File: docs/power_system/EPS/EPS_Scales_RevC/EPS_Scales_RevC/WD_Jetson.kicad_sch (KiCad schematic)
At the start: 40 parts, among them J6 Breakout, J7 Breakout, U3 TLV1704

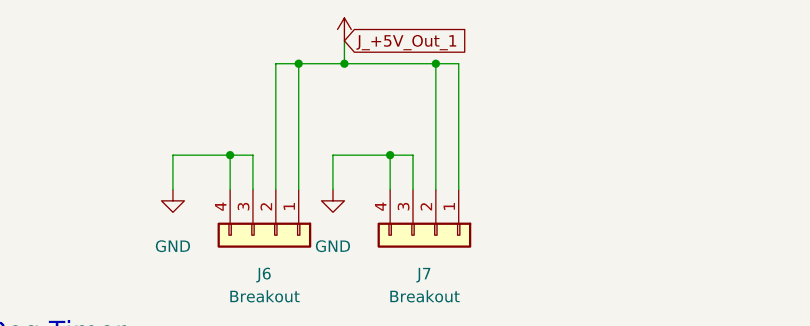
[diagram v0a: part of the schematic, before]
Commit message: Calculations
Lots of behind the scenes stuff going on. Ran through calculations for the Load Switch, Switching Regulator and clock for the jetson using the information from each datasheet. Having to modify these parameters for each subsystem is time consuming as each one requires new calculations. Once this bit is done the schematic will be done, leading to layout. Aiming for thursday Layout.
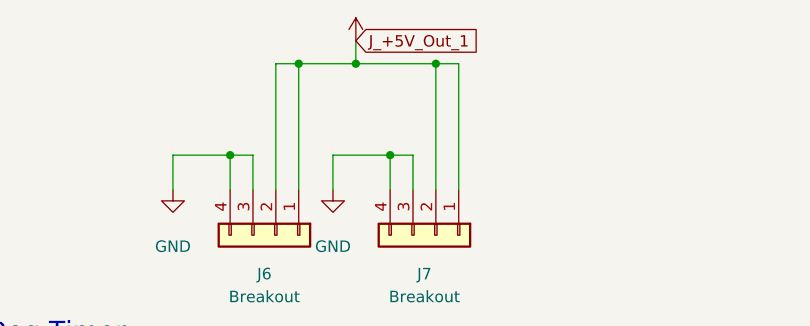
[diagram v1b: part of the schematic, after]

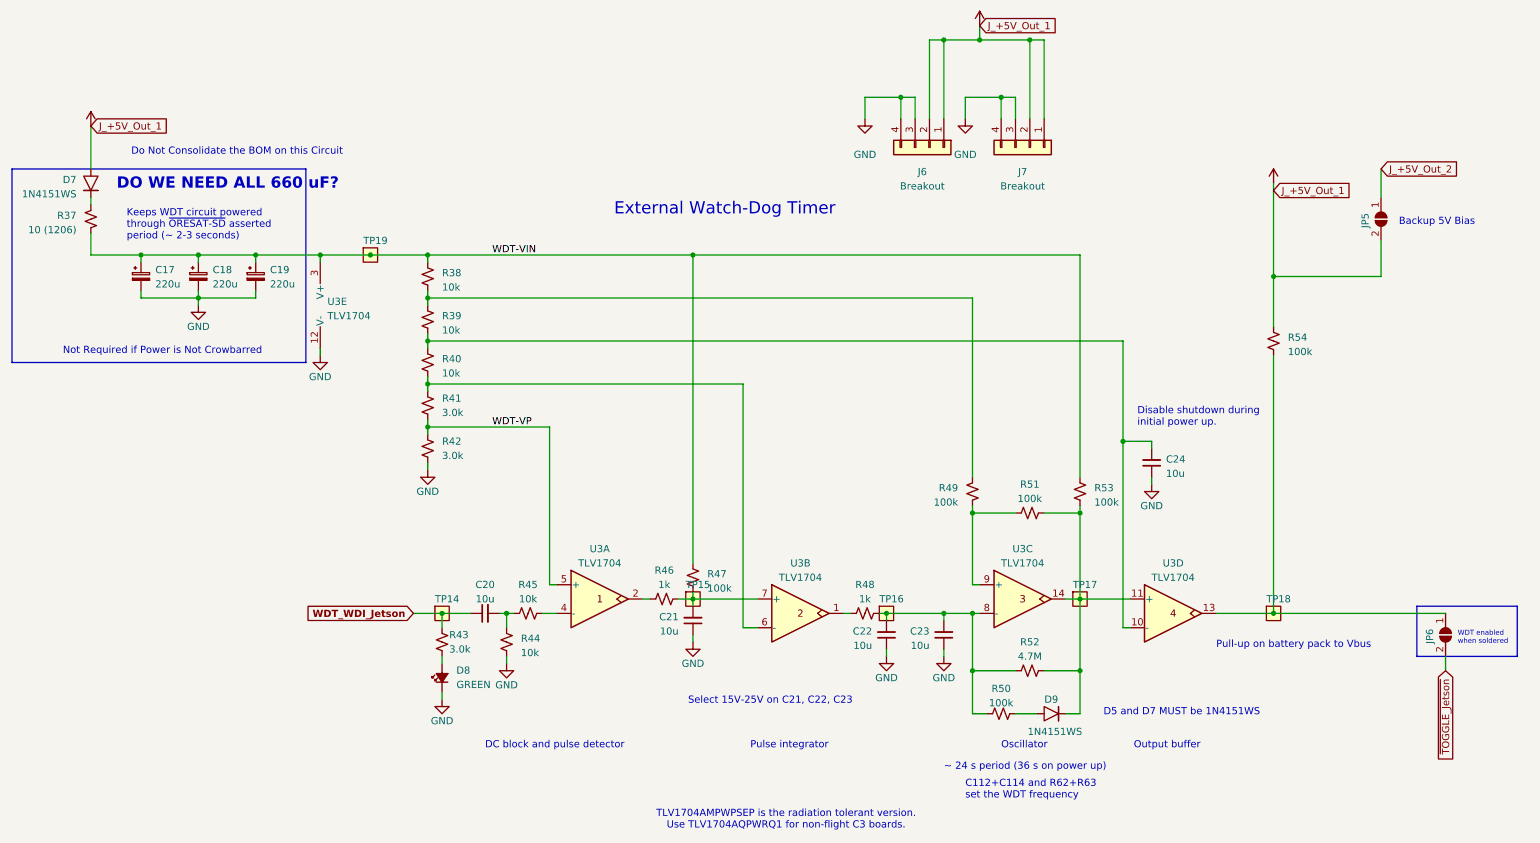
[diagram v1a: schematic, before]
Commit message: Rev C. Schematic 90 % Complete
All EPS components for each subsystem implemented. Only errors and warning are relating to missing peripheral connections and connectors which will be discussed tomorrow when I go to the lab.
Calculations are done as well.
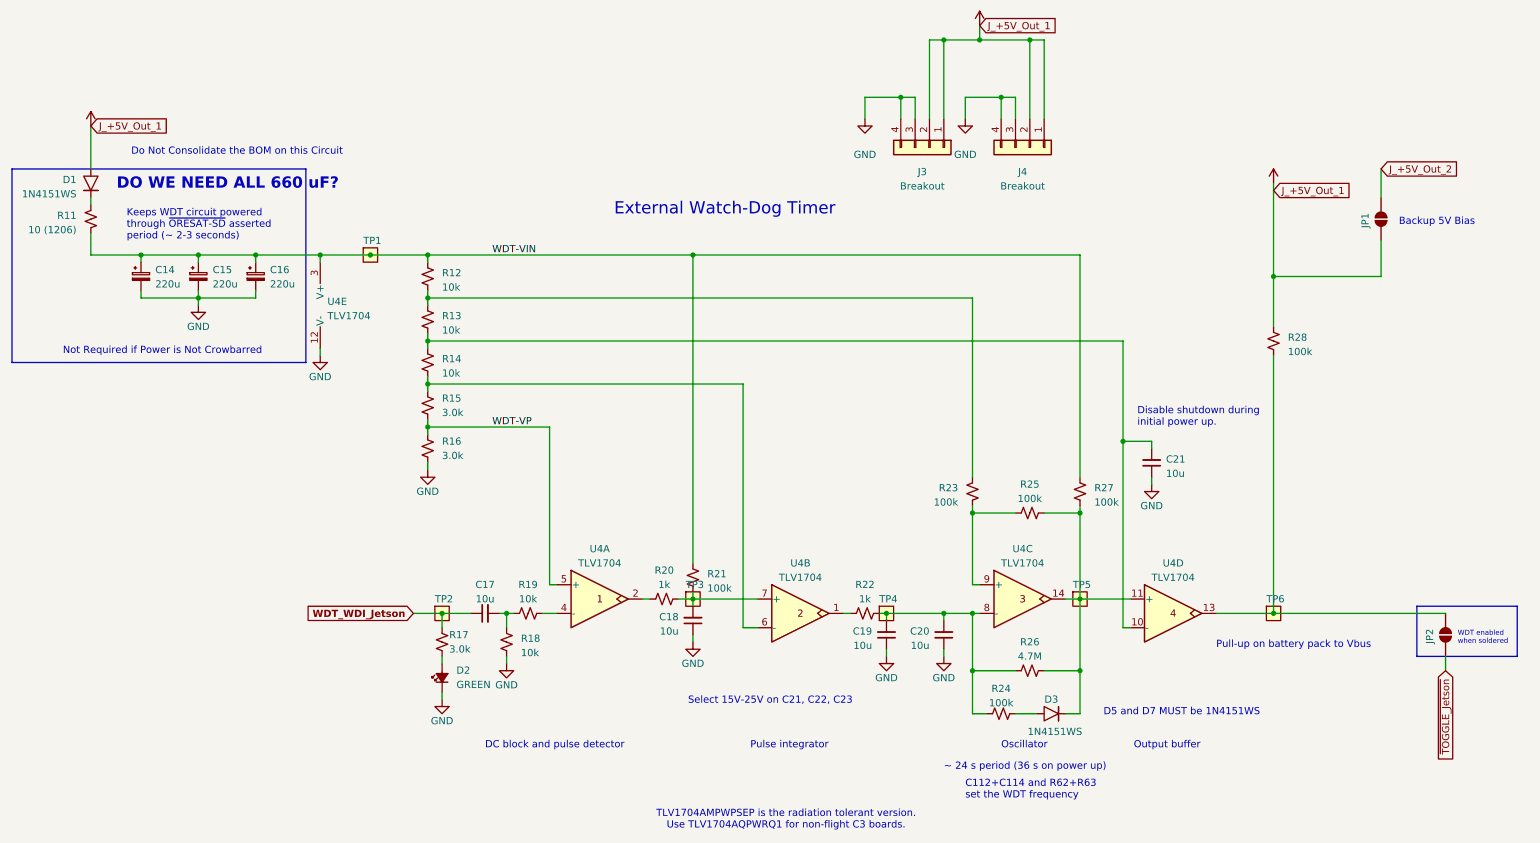
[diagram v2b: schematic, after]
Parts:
- renumbered C17 to C14, C18 to C15, C19 to C16, C20 to C17, C21 to C18, C22 to C19, C23 to C20, C24 to C21, D7 to D1, D8 to D2, D9 to D3, J6 to J3, J7 to J4, JP5 to JP1, JP6 to JP2, R37 to R11, R38 to R12, R39 to R13, R40 to R14, R41 to R15, R42 to R16, R43 to R17, R44 to R18, R45 to R19, R46 to R20, R47 to R21, R48 to R22, R49 to R23, R50 to R24, R51 to R25, R52 to R26, R53 to R27, R54 to R28, TP19 to TP1, TP14 to TP2, TP15 to TP3, TP16 to TP4, TP17 to TP5, TP18 to TP6, U3 to U4

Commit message: Added Dummy Boards & XNOR functionality
Almost done with Dummy boards, just need to link some gecko footprints to the schematic symbol pins and layout can begin
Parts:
- D1, D3: symbol oresat-diodes:1N4151WS-HE3 -> Device:D
- J4: footprint FC_DEV_BOARD:JST_BM04B-SRSS-TB(LF)(SN) -> Connector_PinHeader_2.54mm:PinHeader_1x04_P2.54mm_Vertical
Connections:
- net J_+5V_Out_2 is gone; now on net +5V_ROUT3: JP1.1 (A)
- net ~{TOGGLE_Jetson} renamed ~{WD_TOGGLE_Jetson}
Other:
- note added: "D1 and D7 MUST be 1N4151WS"
- note removed: "D5 and D7 MUST be 1N4151WS"
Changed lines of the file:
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@@
 		)
 	)
-	(text "D5 and D7 MUST be 1N4151WS"
+	(text "D1 and D7 MUST be 1N4151WS"
 		(exclude_from_sim no)
 		(at 222.504 140.716 0)
@@
 	(wire
 		(pts
-			(xy 201.93 140.97) (xy 204.47 140.97)
-		)
-		(stroke
-			(width 0)
-			(type default)
-		)
-	)
-	(wire
-		(pts
 			(xy 88.9 90.17) (xy 88.9 91.44)
 		)
@@
 	(wire
 		(pts
-			(xy 38.1 59.69) (xy 48.26 59.69)
+			(xy 193.04 140.97) (xy 194.31 140.97)
 		)
 		(stroke
@@
 	(wire
 		(pts
-			(xy 177.8 35.56) (xy 177.8 21.59)
+			(xy 38.1 59.69) (xy 48.26 59.69)
 		)
 		(stroke
@@
 	(wire
 		(pts
-			(xy 29.21 36.83) (xy 29.21 44.45)
+			(xy 177.8 35.56) (xy 177.8 21.59)
 		)
 		(stroke
@@
 	(wire
 		(pts
-			(xy 238.76 46.99) (xy 238.76 63.5)
+			(xy 238.76 43.18) (xy 238.76 63.5)
 		)
 		(stroke
@@
 	(wire
 		(pts
+			(xy 201.93 140.97) (xy 204.47 140.97)
+		)
+		(stroke
+			(width 0)
+			(type default)
+		)
+	)
+	(wire
+		(pts
 			(xy 185.42 99.06) (xy 185.42 67.31)
 		)
@@
 	(wire
 		(pts
-			(xy 29.21 49.53) (xy 29.21 50.8)
+			(xy 58.42 60.96) (xy 58.42 59.69)
 		)
 		(stroke
@@
 	(wire
 		(pts
-			(xy 58.42 60.96) (xy 58.42 59.69)
+			(xy 193.04 133.35) (xy 185.42 133.35)
 		)
 		(stroke
@@
 	(wire
 		(pts
-			(xy 193.04 133.35) (xy 185.42 133.35)
+			(xy 69.85 59.69) (xy 78.74 59.69)
 		)
 		(stroke
@@
 	(wire
 		(pts
-			(xy 69.85 59.69) (xy 78.74 59.69)
+			(xy 29.21 36.83) (xy 29.21 41.91)
 		)
 		(stroke
@@
 	(wire
 		(pts
+			(xy 29.21 49.53) (xy 29.21 50.8)
+		)
+		(stroke
+			(width 0)
+			(type default)
+		)
+	)
+	(wire
+		(pts
 			(xy 212.09 74.93) (xy 212.09 92.71)
 		)
@@
 		)
 	)
-	(wire
-		(pts
-			(xy 193.04 140.97) (xy 196.85 140.97)
-		)
-		(stroke
-			(width 0)
-			(type default)
-		)
-	)
 	(polyline
 		(pts
@@
 		)
 	)
-	(global_label "J_+5V_Out_2"
+	(global_label "~{WD_TOGGLE_Jetson}"
 		(shape input)
-		(at 257.81 44.45 0)
+		(at 269.24 133.35 270)
 		(fields_autoplaced yes)
 		(effects
@@
 				(size 1.27 1.27)
 			)
-			(justify left)
+			(justify right)
 		)
 		(property "Intersheetrefs" "${INTERSHEET_REFS}"
-			(at 272.9508 44.45 0)
+			(at 269.24 154.115 90)
 			(effects
 				(font
 					(size 1.27 1.27)
 				)
-				(justify left)
+				(justify right)
 				(hide yes)
 			)
 		)
 	)
-	(global_label "~{TOGGLE_Jetson}"
+	(global_label "J_+5V_Out_1"
 		(shape input)
-		(at 269.24 133.35 270)
+		(at 186.69 19.05 0)
 		(fields_autoplaced yes)
 		(effects
@@
 				(size 1.27 1.27)
 			)
-			(justify right)
+			(justify left)
 		)
 		(property "Intersheetrefs" "${INTERSHEET_REFS}"
-			(at 269.24 150.426 90)
+			(at 201.8308 19.05 0)
 			(effects
 				(font
 					(size 1.27 1.27)
 				)
-				(justify right)
+				(justify left)
 				(hide yes)
 			)
@@
 	(global_label "J_+5V_Out_1"
 		(shape input)
-		(at 186.69 19.05 0)
+		(at 238.76 44.45 0)
 		(fields_autoplaced yes)
 		(effects
@@
 		)
 		(property "Intersheetrefs" "${INTERSHEET_REFS}"
-			(at 201.8308 19.05 0)
+			(at 253.9008 44.45 0)
 			(effects
 				(font
@@
 	(global_label "J_+5V_Out_1"
 		(shape input)
-		(at 238.76 48.26 0)
+		(at 257.81 44.45 0)
 		(fields_autoplaced yes)
 		(effects
@@
 		)
 		(property "Intersheetrefs" "${INTERSHEET_REFS}"
-			(at 253.9008 48.26 0)
+			(at 272.9508 44.45 0)
 			(effects
 				(font
@@
 			)
 		)
-		(property "Footprint" "FC_DEV_BOARD:JST_BM04B-SRSS-TB(LF)(SN)"
+		(property "Footprint" "Connector_PinHeader_2.54mm:PinHeader_1x04_P2.54mm_Vertical"
 			(at 195.58 40.64 0)
 			(effects
@@
 	)
 	(symbol
-		(lib_id "oresat-diodes:1N4151WS-HE3")
-		(at 29.21 46.99 90)
+		(lib_id "Device:D")
+		(at 29.21 45.72 270)
 		(mirror x)
 		(unit 1)
@@
 		(dnp no)
 		(property "Reference" "D1"
-			(at 26.67 46.355 90)
+			(at 31.75 46.355 90)
 			(effects
 				(font
@@
 		)
 		(property "Value" "1N4151WS"
-			(at 26.67 48.895 90)
+			(at 31.75 43.815 90)
 			(effects
 				(font
@@
 		)
 		(property "Footprint" "Diode_SMD:D_SOD-323"
-			(at 34.29 46.99 0)
+			(at 29.21 45.72 0)
 			(effects
 				(font
@@
 			)
 		)
-		(property "Datasheet" "https://www.vishay.com/docs/85847/1n4151ws.pdf"
-			(at 36.83 46.99 0)
+		(property "Datasheet" "~"
+			(at 29.21 45.72 0)
 			(effects
 				(font
@@
 			)
 		)
-		(property "Description" "Diode Standard 50V 150mA Surface Mount SOD-323"
-			(at 29.21 46.99 0)
+		(property "Description" "Diode"
+			(at 29.21 45.72 0)
 			(effects
 				(font
@@
 		)
 		(property "DPN" "112-1N4151WS-E3-08CT-ND"
-			(at 29.21 46.99 0)
+			(at 29.21 45.72 0)
 			(effects
 				(font
@@
 		)
 		(property "DST" "Digi-Key"
-			(at 29.21 46.99 0)
+			(at 29.21 45.72 0)
 			(effects
 				(font
@@
 		)
 		(property "MFR" "Vishay"
-			(at 29.21 46.99 0)
+			(at 29.21 45.72 0)
 			(effects
 				(font
@@
 		)
 		(property "MPN" "1N4151WS-E3-08"
-			(at 29.21 46.99 0)
+			(at 29.21 45.72 0)
+			(effects
+				(font
+					(size 1.27 1.27)
+				)
+				(hide yes)
+			)
+		)
+		(property "Sim.Device" "D"
+			(at 29.21 45.72 0)
+			(effects
+				(font
+					(size 1.27 1.27)
+				)
+				(hide yes)
+			)
+		)
+		(property "Sim.Pins" "1=K 2=A"
+			(at 29.21 45.72 0)
 			(effects
 				(font
@@
 	(symbol
 		(lib_id "power:VBUS")
-		(at 238.76 46.99 0)
+		(at 238.76 43.18 0)
 		(unit 1)
 		(exclude_from_sim no)
@@
 		(fields_autoplaced yes)
 		(property "Reference" "#PWR027"
-			(at 238.76 50.8 0)
+			(at 238.76 46.99 0)
 			(effects
 				(font
@@
 		)
 		(property "Value" "+5V_ROUT3"
-			(at 241.3 45.7199 0)
+			(at 241.3 41.9099 0)
 			(effects
 				(font
@@
 		)
 		(property "Footprint" ""
-			(at 238.76 46.99 0)
+			(at 238.76 43.18 0)
 			(effects
 				(font
@@
 		)
 		(property "Datasheet" ""
-			(at 238.76 46.99 0)
+			(at 238.76 43.18 0)
 			(effects
 				(font
@@
 		)
 		(property "Description" "Power symbol creates a global label with name \"VBUS\""
-			(at 238.76 46.99 0)
+			(at 238.76 43.18 0)
 			(effects
 				(font
@@
 	)
 	(symbol
-		(lib_id "oresat-diodes:1N4151WS-HE3")
-		(at 199.39 140.97 0)
+		(lib_id "Device:D")
+		(at 198.12 140.97 180)
 		(unit 1)
 		(exclude_from_sim no)
@@
 		(dnp no)
 		(property "Reference" "D3"
-			(at 199.39 138.43 0)
+			(at 198.12 143.51 0)
 			(effects
 				(font
@@
 		)
 		(property "Value" "1N4151WS"
-			(at 200.025 144.145 0)
+			(at 198.882 138.43 0)
 			(effects
 				(font
@@
 		)
 		(property "Footprint" "Diode_SMD:D_SOD-323"
-			(at 199.39 146.05 0)
+			(at 198.12 140.97 0)
 			(effects
 				(font
@@
 			)
 		)
-		(property "Datasheet" "https://www.vishay.com/docs/85847/1n4151ws.pdf"
-			(at 199.39 148.59 0)
+		(property "Datasheet" "~"
+			(at 198.12 140.97 0)
 			(effects
 				(font
@@
 			)
 		)
-		(property "Description" "Diode Standard 50V 150mA Surface Mount SOD-323"
-			(at 199.39 140.97 0)
+		(property "Description" "Diode"
+			(at 198.12 140.97 0)
 			(effects
 				(font
@@
 		)
 		(property "DPN" "112-1N4151WS-E3-08CT-ND"
-			(at 199.39 140.97 0)
+			(at 198.12 140.97 0)
 			(effects
 				(font
@@
 		)
 		(property "DST" "Digi-Key"
-			(at 199.39 140.97 0)
+			(at 198.12 140.97 0)
 			(effects
 				(font
@@
 		)
 		(property "MFR" "Vishay"
-			(at 199.39 140.97 0)
+			(at 198.12 140.97 0)
 			(effects
 				(font
@@
 		)
 		(property "MPN" "1N4151WS-E3-08"
-			(at 199.39 140.97 0)
+			(at 198.12 140.97 0)
+			(effects
+				(font
+					(size 1.27 1.27)
+				)
+				(hide yes)
+			)
+		)
+		(property "Sim.Device" "D"
+			(at 198.12 140.97 0)
+			(effects
+				(font
+					(size 1.27 1.27)
+				)
+				(hide yes)
+			)
+		)
+		(property "Sim.Pins" "1=K 2=A"
+			(at 198.12 140.97 0)
 			(effects
 				(font

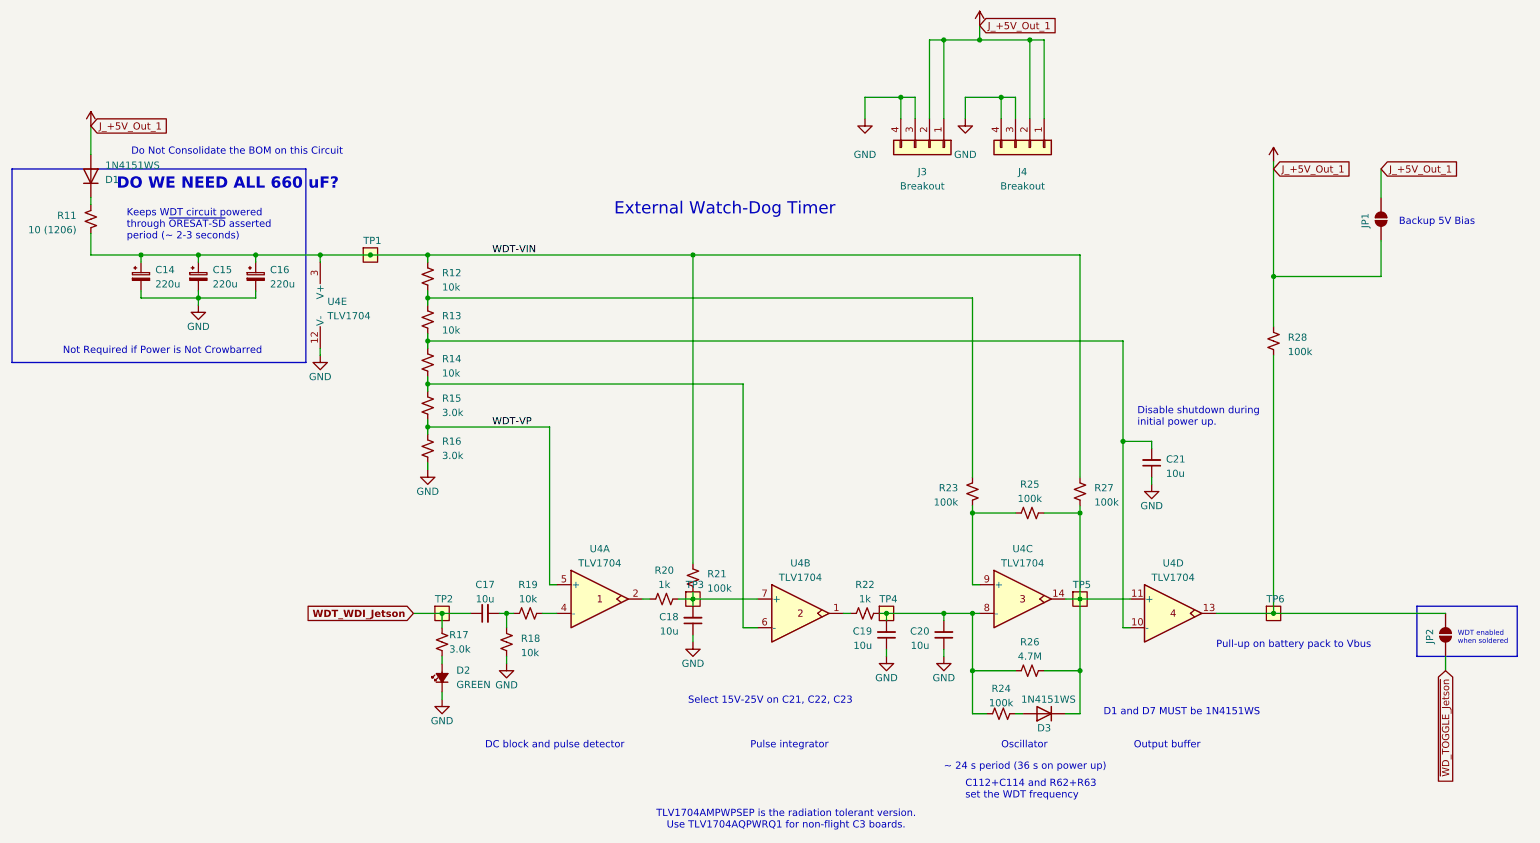
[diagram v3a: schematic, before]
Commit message: Rev C. Layout Started
Footprints and Symbols properly linked. Started organizing PCB layout
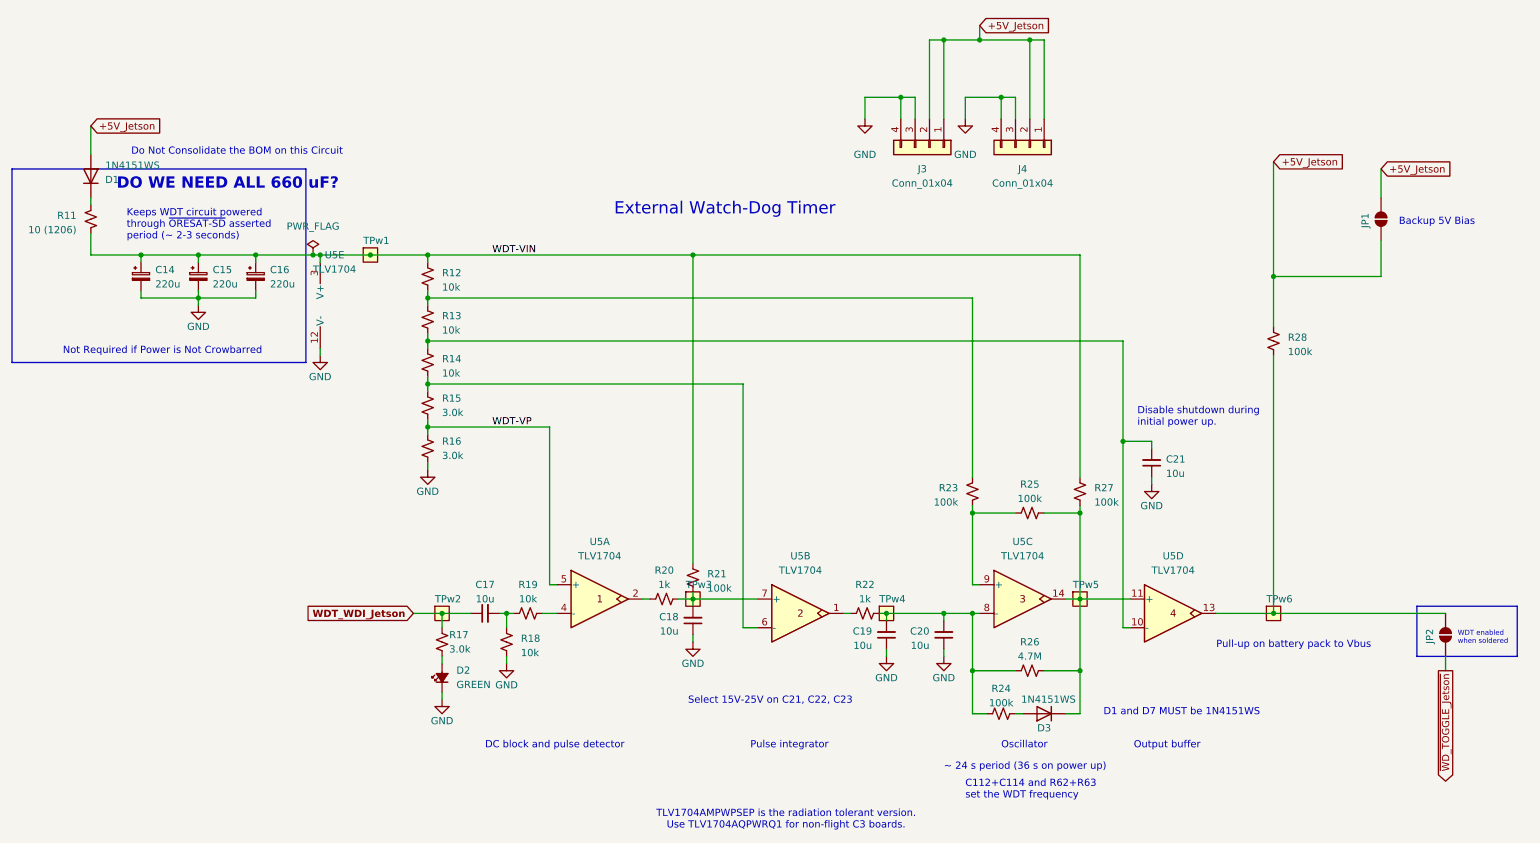
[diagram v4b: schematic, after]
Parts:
- J3, J4: value Breakout -> Conn_01x04; footprint Connector_PinHeader_2.54mm:PinHeader_1x04_P2.54mm_Vertical -> Connector_PinSocket_2.54mm:PinSocket_1x04_P2.54mm_Vertical
- TPw1: renamed from TP1; symbol oresat-misc:Test-Point-0.75mm-th -> TestPointWD:Test-Point-0.75mm-th
- TPw2: renamed from TP2; symbol oresat-misc:Test-Point-0.75mm-th -> TestPointWD:Test-Point-0.75mm-th
- TPw3: renamed from TP3; symbol oresat-misc:Test-Point-0.75mm-th -> TestPointWD:Test-Point-0.75mm-th
- TPw4: renamed from TP4; symbol oresat-misc:Test-Point-0.75mm-th -> TestPointWD:Test-Point-0.75mm-th
- TPw5: renamed from TP5; symbol oresat-misc:Test-Point-0.75mm-th -> TestPointWD:Test-Point-0.75mm-th
- TPw6: renamed from TP6; symbol oresat-misc:Test-Point-0.75mm-th -> TestPointWD:Test-Point-0.75mm-th
- U5: renamed from U4; symbol oresat-ics:TLV1704AIPWR -> TLV1704:TLV1704AIPWR
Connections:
- net +5V_ROUT3 renamed +5V_Jetson
